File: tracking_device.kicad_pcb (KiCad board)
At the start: 4 copper layers, 68.9 x 77 mm, 81 parts, among them J1 USB_OTG, J2 CONN_01X02, J3 CONN_01X02, J4 CONN_01X02, J5 CONN_01X02, J6 JST-PH, J7 Micro_SD_Connector, J8 CONN_01X06, J9 CONN_01X03, Q1 Si2343DS, SW1 PUSH, SW2 PUSH, SW3 SW_Push, U1 RClamp0503F, U2 SAM-M8, U3 MCP73831, U4 STC3100, U5 REG113NA-3.3, U6 STM32L476RG, U7 RFM95W, Y1 ABS07-120-32.768kHz-T

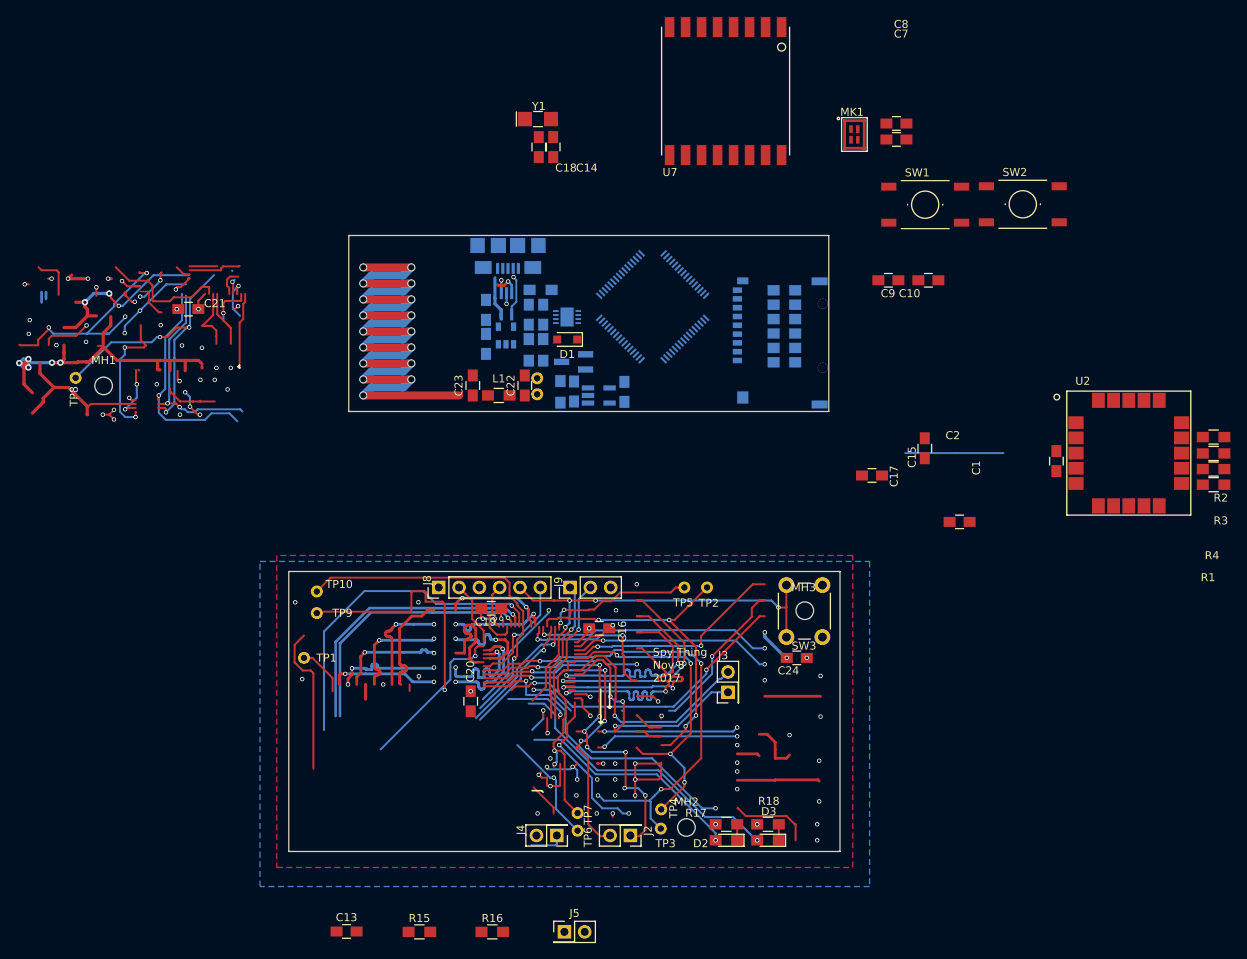
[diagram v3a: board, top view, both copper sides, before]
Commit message: Rev 3 DRC clean
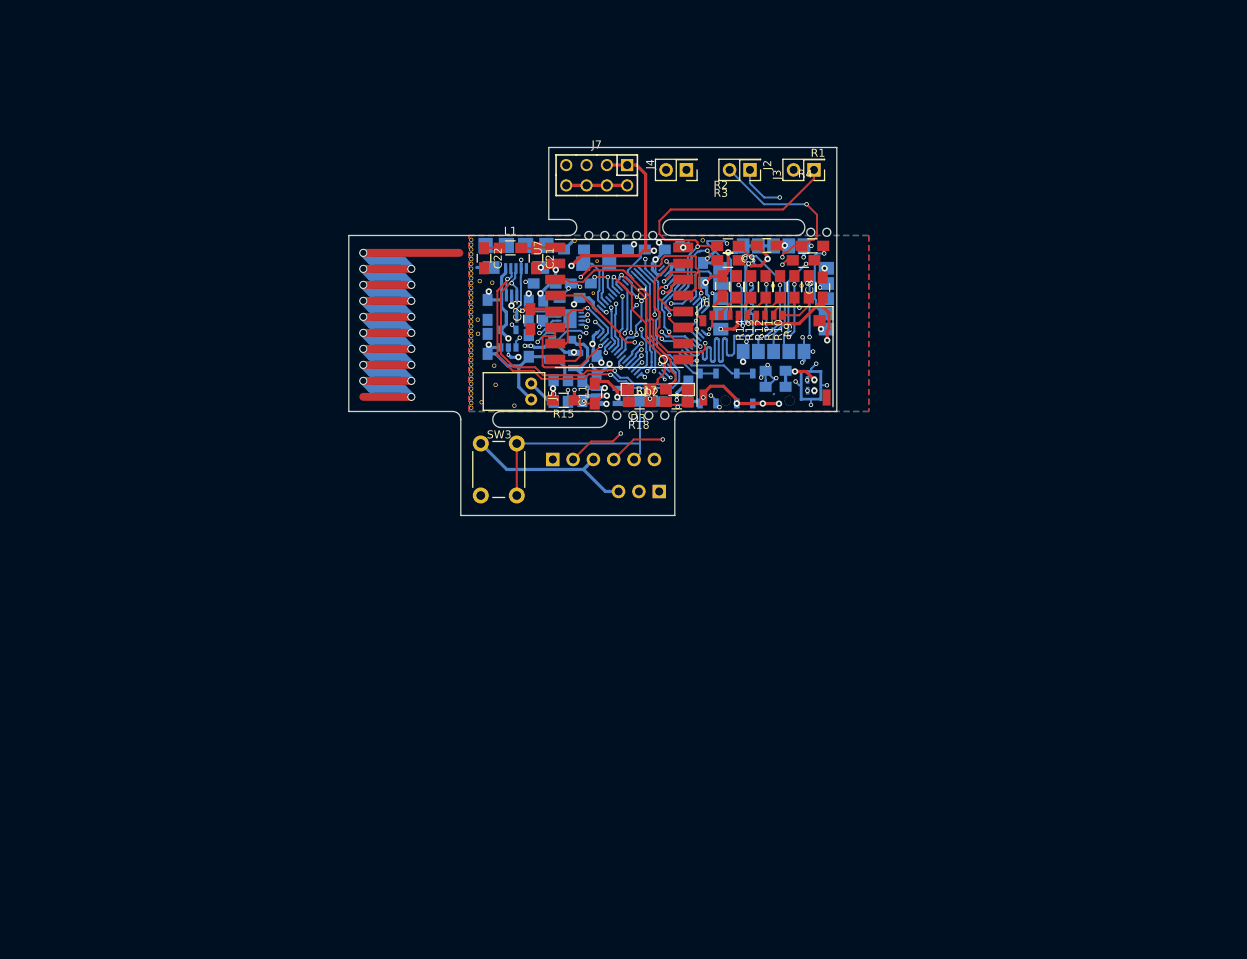
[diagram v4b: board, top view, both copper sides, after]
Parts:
- removed the C2 at (176.3, 73.8)
- removed the J5 at (127.0, 125.1)
- removed MH1, MH2, MH3: MOUNTING_HOLE, Mounting_Holes:MountingHole_2.2mm_M2
- removed TP1, TP10, TP2, TP3, TP4, TP5, TP6, TP7, TP8, TP9: TEST, Measurement_Points:Measurement_Point_Round-TH_Small
- added ?: , tracking_device:VIA_0.35mm_0.55mm, F.Cu at (130.6, 45.2)
- added ?: , tracking_device:VIA_0.35mm_0.55mm, F.Cu at (116.2, 50.3)
- added ?: , tracking_device:VIA_0.35mm_0.55mm, F.Cu at (118.2, 54.3)
- added ?: , tracking_device:VIA_0.35mm_0.55mm, F.Cu at (116.6, 58.9)
- added ?: , tracking_device:VIA_0.35mm_0.55mm, F.Cu at (118.3, 56.7)
- added ?: , tracking_device:VIA_0.35mm_0.55mm, F.Cu at (120.7, 59.3)
- added ?: , tracking_device:VIA_0.35mm_0.55mm, F.Cu at (115.3, 59.5)
- added ?: , tracking_device:VIA_0.35mm_0.55mm, F.Cu at (115.3, 59.0)
- added ?: , tracking_device:VIA_0.35mm_0.55mm, F.Cu at (115.3, 58.4)
- added ?: , tracking_device:VIA_0.35mm_0.55mm, F.Cu at (115.3, 57.8)
- added ?: , tracking_device:VIA_0.35mm_0.55mm, F.Cu at (115.3, 57.1)
- added ?: , tracking_device:VIA_0.35mm_0.55mm, F.Cu at (131.0, 41.2)
- added ?: , tracking_device:VIA_0.35mm_0.55mm, F.Cu at (115.3, 56.5)
- added ?: , tracking_device:VIA_0.35mm_0.55mm, F.Cu at (115.3, 56.0)
- added ?: , tracking_device:VIA_0.35mm_0.55mm, F.Cu at (115.3, 55.4)
- added ?: , tracking_device:VIA_0.35mm_0.55mm, F.Cu at (115.3, 54.8)
- added ?: , tracking_device:VIA_0.35mm_0.55mm, F.Cu at (115.3, 54.1)
- added ?: , tracking_device:VIA_0.35mm_0.55mm, F.Cu at (115.3, 53.5)
- added ?: , tracking_device:VIA_0.35mm_0.55mm, F.Cu at (115.3, 53.0)
- added ?: , tracking_device:VIA_0.35mm_0.55mm, F.Cu at (115.3, 52.4)
- added ?: , tracking_device:VIA_0.35mm_0.55mm, F.Cu at (115.3, 51.8)
- added ?: , tracking_device:VIA_0.35mm_0.55mm, F.Cu at (115.3, 51.1)
- added ?: , tracking_device:VIA_0.35mm_0.55mm, F.Cu at (144.2, 38.6)
- added ?: , tracking_device:VIA_0.35mm_0.55mm, F.Cu at (115.3, 50.5)
- added ?: , tracking_device:VIA_0.35mm_0.55mm, F.Cu at (115.3, 50.0)
- added ?: , tracking_device:VIA_0.35mm_0.55mm, F.Cu at (115.3, 49.4)
- added ?: , tracking_device:VIA_0.35mm_0.55mm, F.Cu at (115.3, 48.8)
- added ?: , tracking_device:VIA_0.35mm_0.55mm, F.Cu at (115.3, 48.1)
- added ?: , tracking_device:VIA_0.35mm_0.55mm, F.Cu at (115.3, 47.5)
- added ?: , tracking_device:VIA_0.35mm_0.55mm, F.Cu at (115.3, 47.0)
- added ?: , tracking_device:VIA_0.35mm_0.55mm, F.Cu at (115.3, 46.4)
- added ?: , tracking_device:VIA_0.35mm_0.55mm, F.Cu at (115.3, 45.8)
- added ?: , tracking_device:VIA_0.35mm_0.55mm, F.Cu at (115.3, 45.1)
- added ?: , tracking_device:VIA_0.35mm_0.55mm, F.Cu at (156.6, 44.3)
- added ?: , tracking_device:VIA_0.35mm_0.55mm, F.Cu at (115.3, 44.5)
- added ?: , tracking_device:VIA_0.35mm_0.55mm, F.Cu at (115.3, 44.0)
- added ?: , tracking_device:VIA_0.35mm_0.55mm, F.Cu at (115.3, 43.4)
- added ?: , tracking_device:VIA_0.35mm_0.55mm, F.Cu at (115.3, 42.8)
- added ?: , tracking_device:VIA_0.35mm_0.55mm, F.Cu at (115.3, 42.1)
- added ?: , tracking_device:VIA_0.35mm_0.55mm, F.Cu at (115.3, 41.5)
- added ?: , tracking_device:VIA_0.35mm_0.55mm, F.Cu at (115.3, 41.0)
- added ?: , tracking_device:VIA_0.35mm_0.55mm, F.Cu at (115.3, 40.4)
- added ?: , tracking_device:VIA_0.35mm_0.55mm, F.Cu at (115.3, 39.8)
- added ?: , tracking_device:VIA_0.35mm_0.55mm, F.Cu at (115.3, 39.1)
- added ?: , tracking_device:VIA_0.35mm_0.55mm, F.Cu at (153.0, 44.3)
- added ?: , tracking_device:VIA_0.35mm_0.55mm, F.Cu at (115.3, 38.5)
- added ?: , tracking_device:VIA_0.35mm_0.55mm, F.Cu at (128.2, 38.6)
- added ?: , tracking_device:VIA_0.35mm_0.55mm, F.Cu at (116.4, 43.7)
- added ?: , tracking_device:VIA_0.35mm_0.55mm, F.Cu at (117.9, 43.9)
- added ?: , tracking_device:VIA_0.35mm_0.55mm, F.Cu at (116.1, 48.5)
- added J7: CONN_02X04, tracking_device:HEADER_M_2.54MM_2R8P_ST_AU_PTH, F.Cu at (131.0, 30.5)
- added REF**: mouse_bite, tracking_device:mouse_bite, F.Cu at (159.8, 37.6)
- added REF**: mouse_bite, tracking_device:mouse_bite, F.Cu at (137.5, 60.5)
- added REF**: mouse_bite, tracking_device:mouse_bite, F.Cu at (139.5, 60.5)
- added REF**: mouse_bite, tracking_device:mouse_bite, F.Cu at (157.8, 37.6)
- added REF**: mouse_bite, tracking_device:mouse_bite, F.Cu at (138.0, 38.0)
- added REF**: mouse_bite, tracking_device:mouse_bite, F.Cu at (136.0, 38.0)
- added REF**: mouse_bite, tracking_device:mouse_bite, F.Cu at (134.0, 38.0)
- added REF**: mouse_bite, tracking_device:mouse_bite, F.Cu at (132.0, 38.0)
- added REF**: mouse_bite, tracking_device:mouse_bite, F.Cu at (130.0, 38.0)
- added REF**: mouse_bite, tracking_device:mouse_bite, F.Cu at (133.5, 60.5)
- added REF**: mouse_bite, tracking_device:mouse_bite, F.Cu at (135.5, 60.5)
- C1: value DNI -> 100n
- C11: renamed from C12; moved to F.Cu
- C12: renamed from C13; moved to B.Cu
- C13: renamed from C14; moved to B.Cu
- C14: renamed from C15; moved to B.Cu
- C15: renamed from C16; moved to B.Cu
- C16: renamed from C17; moved to B.Cu
- C17: renamed from C18; moved to B.Cu
- C18: renamed from C19; moved to B.Cu
- C19: renamed from C20; moved to B.Cu
- C20: renamed from C21; moved to B.Cu
- C6: renamed from C7; moved to B.Cu
- C7: renamed from C8; moved to B.Cu
- D1, J8, J9, MK1, R16, U2, Y1: moved to B.Cu
- J5: renamed from J6; moved to F.Cu
- J6: renamed from J7; moved to F.Cu
- R10, R11, R12, R13, R14, R9: moved to F.Cu
- SW1, SW2: footprint tracking_device:K2-1102SP-I4SC-04 -> tracking_device:SW_3.1x3.1; moved to B.Cu
- moved C12 86.1 mm to (129.0, 44.0), turned to 180 degrees
- moved J4 84.8 mm to (142.2, 29.8)
- moved J2 84.5 mm to (150.1, 29.8)
- moved R16 69.2 mm to (137.8, 58.8), turned to 180 degrees
- moved R15 68.9 mm to (126.8, 58.6), turned to 180 degrees
- moved J3 66.2 mm to (158.1, 29.8), turned to 180 degrees
- moved R3 65.3 mm to (147.4, 41.1), turned to 0 degrees
- moved R2 65.2 mm to (147.4, 39.3), turned to 0 degrees
- moved C20 64.5 mm to (144.3, 42.7), turned to 90 degrees
- moved C19 61.0 mm to (138.2, 39.8), turned to 0 degrees
- moved D3 58.6 mm to (136.2, 57.2), turned to 0 degrees
- moved R1 58.4 mm to (157.9, 39.3), turned to 0 degrees
- moved R4 57.5 mm to (156.8, 41.1), turned to 0 degrees
- moved D2 56.7 mm to (141.0, 57.2)
- moved R18 55.2 mm to (136.3, 58.8), turned to 0 degrees
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- renumbered C11 to C10, C3 to C2, C22 to C21, C23 to C22, C24 to C23, C4 to C3, C5 to C4, C6 to C5, C9 to C8, C10 to C9
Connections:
- net Net-(C11-Pad2) renamed /VIN
- C21 pad 2: /SX1272/RADIO_GND -> GND
- C22 pad 2: /SX1272/RADIO_GND -> GND
- C23 pad 2: /SX1272/RADIO_GND -> GND
- U2 pad 8: Net-(U2-Pad8) -> (no net)
- U4 pad 1: Net-(U4-Pad1) -> (no net)
- U5 pad 4: Net-(U5-Pad4) -> (no net)
- U6 pad 11: /Microcontroller/SWITCH_1 -> (no net)
- U6 pad 17: /Microcontroller/SWITCH_2 -> (no net)
- U6 pad 26: Net-(U6-Pad26) -> (no net)
- U6 pad 41: Net-(U6-Pad41) -> /Microcontroller/SWITCH_1
- U6 pad 42: /PMIC_FAST -> /Microcontroller/SWITCH_2
- U6 pad 5: Net-(U6-Pad5) -> (no net)
- U6 pad 6: Net-(U6-Pad6) -> (no net)
- U7 pad 1: /SX1272/RADIO_GND -> GND
- U7 pad 10: /SX1272/RADIO_GND -> GND
- U7 pad 8: /SX1272/RADIO_GND -> GND
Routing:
- net (no net): track 1288.5 -> 127.5 mm, vias 176 -> 19
- net VDD: track 14.0 -> 214.9 mm, vias 6 -> 19
- net GND: track 9.79 -> 169.5 mm, vias 7 -> 53
- net /VBAT: track 0.00 -> 55.3 mm, vias 0 -> 1
- net /VUSB: track 32.6 -> 77.9 mm, vias 2 -> 8
- net /PMIC_FAST: track 43.7 -> 0.00 mm, vias 1 -> 0
- net /PMIC_I2C_SDA: track 0.00 -> 42.7 mm, vias 0 -> 2
- net /PMIC_I2C_SCL: track 4.33 -> 46.1 mm, vias 0 -> 2
- net /USB_D-: track 1.62 -> 41.7 mm, vias 1 -> 2
- net /GPS_RESET_N: track 60.4 -> 20.4 mm, vias 4 -> 3
- net /USB_D+: track 3.19 -> 39.7 mm, vias 1 -> 2
- net /SX1272/DIO2: track 0.00 -> 36.3 mm, vias 0 -> 3
- net /SX1272/DIO3: track 0.00 -> 35.3 mm, vias 0 -> 2
- net /USB_ID: track 5.12 -> 40.3 mm, vias 1 -> 2
- net /Microcontroller/SDMMC_D1: track 0.00 -> 35.1 mm, vias 0 -> 3
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- added copper zone on Inner1, net GND
- added copper zone on Inner2, net GND
- removed copper zone on Ground, net GND
- removed copper zone on Power, net VDD
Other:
- board size 68.9 x 77 mm -> 61 x 46 mm
- net class 50 ohm: clearance 0.16 -> 0.155; trace_width 0.35 -> 0.25
- net class Default: clearance 0.16 -> 0.155
- net class USB: clearance 0.16 -> 0.155; trace_width 0.3 -> 0.25
- net class power: clearance 0.16 -> 0.2
- rule trace_clearance: 0.16 -> 0.155
- rule via_min_size: 0.55 -> 0.3
- board text removed: "Spy Thing Nov 8 2017"
